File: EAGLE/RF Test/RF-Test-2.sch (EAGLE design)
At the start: 9 parts, among them X1 SMA-142-0701-881/886, X2 IPEX-20279-001E

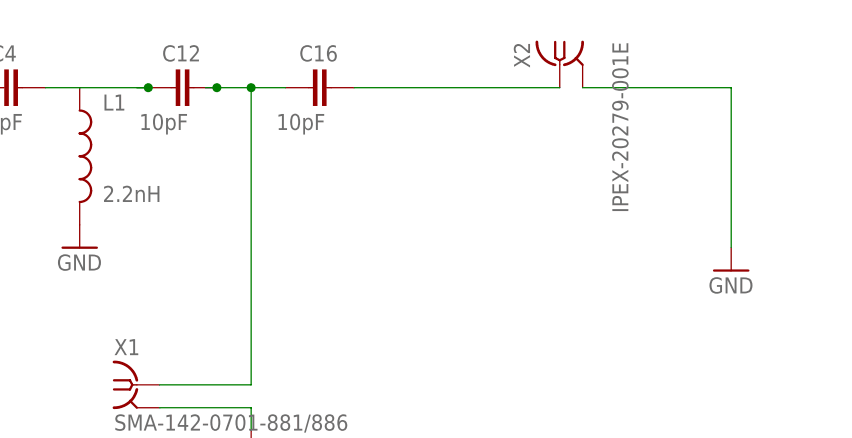
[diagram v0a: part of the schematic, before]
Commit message: RF Test board updated to match. A0 silk screen moved on core.
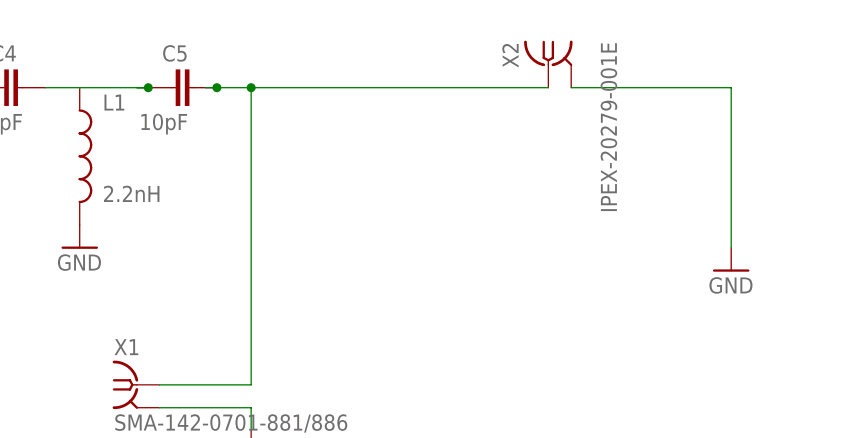
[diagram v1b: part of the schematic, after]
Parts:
- removed C16: 10pF, rcl:C-EUC0603
- renumbered C12 to C5
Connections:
- removed net N$2: C16.2, X2.1
- net N$4: now also X2.1; no longer C16.1
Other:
- moved on the sheet: X2
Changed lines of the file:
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@@
 <class number="1" name="vcc" width="0" drill="0">
 </class>
-<class number="2" name="RF" width="0.5842" drill="0">
-<clearance class="2" value="0.762"/>
+<class number="2" name="RF" width="0.635" drill="0">
+<clearance class="2" value="0.635"/>
 </class>
 <class number="3" name="RF2" width="0.5842" drill="0">
@@
 <part name="GND2" library="SparkFun" deviceset="GND" device=""/>
 <part name="X2" library="Spark" deviceset="IPEX-20279-001E" device=""/>
-<part name="C16" library="rcl" deviceset="C-EU" device="C0603" value="10pF"/>
 <part name="GND20" library="SparkFun" deviceset="GND" device=""/>
 <part name="ANT1" library="Spark" deviceset="AT8010" device=""/>
-<part name="C12" library="rcl" deviceset="C-EU" device="C0603" value="10pF"/>
+<part name="C5" library="rcl" deviceset="C-EU" device="C0603" value="10pF"/>
 <part name="X1" library="andyw-oct-2011" deviceset="SMA-" device="142-0701-881/886"/>
 <part name="GND1" library="SparkFun" deviceset="GND" device=""/>
@@
 </instance>
 <instance part="GND2" gate="1" x="113.03" y="104.14"/>
-<instance part="X2" gate="G$1" x="166.37" y="124.46" rot="MR270"/>
-<instance part="C16" gate="G$1" x="138.43" y="121.92" smashed="yes" rot="R90">
-<attribute name="NAME" x="137.414" y="124.841" size="1.778" layer="95"/>
-<attribute name="VALUE" x="134.874" y="117.221" size="1.778" layer="96"/>
-</instance>
+<instance part="X2" gate="G$1" x="165.1" y="124.46" rot="MR270"/>
 <instance part="GND20" gate="1" x="185.42" y="101.6"/>
 <instance part="ANT1" gate="G$1" x="92.71" y="121.92" rot="R90"/>
-<instance part="C12" gate="G$1" x="123.19" y="121.92" smashed="yes" rot="R90">
+<instance part="C5" gate="G$1" x="123.19" y="121.92" smashed="yes" rot="R90">
 <attribute name="NAME" x="122.174" y="124.841" size="1.778" layer="95"/>
 <attribute name="VALUE" x="119.634" y="117.221" size="1.778" layer="96"/>
@@
 <pinref part="X2" gate="G$1" pin="GND@1"/>
 <pinref part="GND20" gate="1" pin="GND"/>
-<wire x1="168.91" y1="121.92" x2="185.42" y2="121.92" width="0.1524" layer="91"/>
+<wire x1="167.64" y1="121.92" x2="185.42" y2="121.92" width="0.1524" layer="91"/>
 <wire x1="185.42" y1="121.92" x2="185.42" y2="104.14" width="0.1524" layer="91"/>
 </segment>
@@
 </segment>
 </net>
-<net name="N$4" class="3">
+<net name="N$4" class="2">
 <segment>
 <wire x1="132.08" y1="88.9" x2="132.08" y2="121.92" width="0.1524" layer="91"/>
-<pinref part="C16" gate="G$1" pin="1"/>
-<wire x1="135.89" y1="121.92" x2="132.08" y2="121.92" width="0.1524" layer="91"/>
 <wire x1="127" y1="121.92" x2="128.27" y2="121.92" width="0.1524" layer="91"/>
-<junction x="132.08" y="121.92"/>
-<pinref part="C12" gate="G$1" pin="2"/>
+<pinref part="C5" gate="G$1" pin="2"/>
 <wire x1="128.27" y1="121.92" x2="132.08" y2="121.92" width="0.1524" layer="91"/>
 <junction x="128.27" y="121.92"/>
 <pinref part="X1" gate="G1" pin="1"/>
 <wire x1="121.92" y1="88.9" x2="132.08" y2="88.9" width="0.1524" layer="91"/>
+<pinref part="X2" gate="G$1" pin="1"/>
+<wire x1="165.1" y1="121.92" x2="132.08" y2="121.92" width="0.1524" layer="91"/>
+<junction x="132.08" y="121.92"/>
 </segment>
 </net>
@@
 <wire x1="53.34" y1="68.58" x2="66.04" y2="68.58" width="0.1524" layer="91"/>
 <label x="60.96" y="68.58" size="1.778" layer="95"/>
-</segment>
-</net>
-<net name="N$2" class="2">
-<segment>
-<pinref part="C16" gate="G$1" pin="2"/>
-<pinref part="X2" gate="G$1" pin="1"/>
-<wire x1="143.51" y1="121.92" x2="166.37" y2="121.92" width="0.1524" layer="91"/>
 </segment>
 </net>
@@
 <wire x1="109.22" y1="121.92" x2="113.03" y2="121.92" width="0.1524" layer="91"/>
 <wire x1="119.38" y1="121.92" x2="120.65" y2="121.92" width="0.1524" layer="91"/>
-<pinref part="C12" gate="G$1" pin="1"/>
+<pinref part="C5" gate="G$1" pin="1"/>
 <wire x1="120.65" y1="121.92" x2="113.03" y2="121.92" width="0.1524" layer="91"/>
 <junction x="120.65" y="121.92"/>

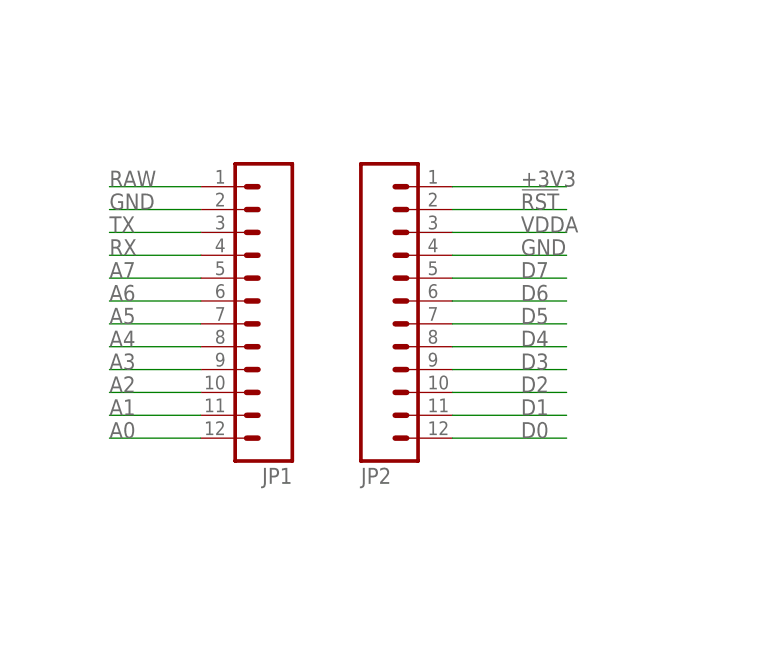
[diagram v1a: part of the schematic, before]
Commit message: Reduce stripline length, shorten test board.
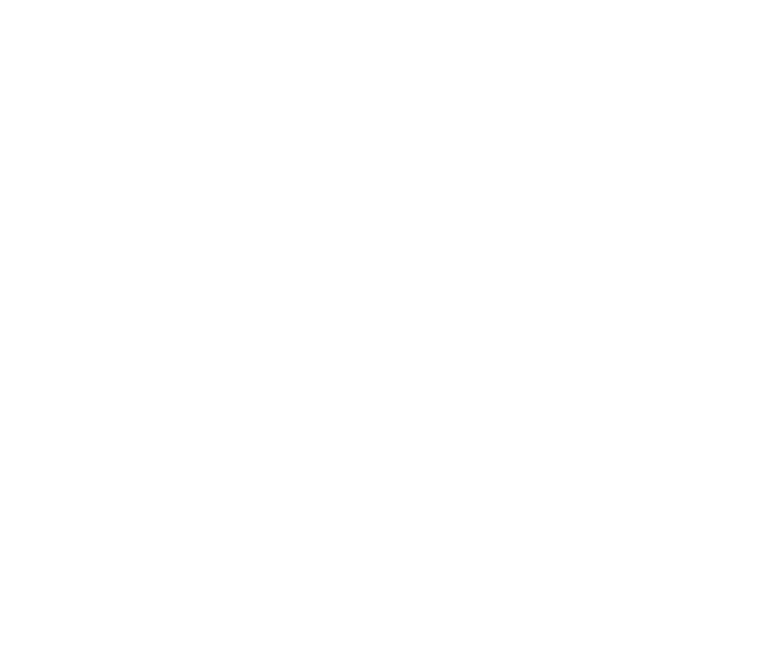
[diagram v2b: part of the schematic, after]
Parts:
- removed JP1, JP2: M12PTH, SparkFun:M12PTH
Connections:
- removed net !RST: JP2.2
- removed net +3V3: JP2.1
- removed net A0: JP1.12
- removed net A1: JP1.11
- removed net A2: JP1.10
- removed net A3: JP1.9
- removed net A4: JP1.8
- removed net A5: JP1.7
- removed net A6: JP1.6
- removed net A7: JP1.5
- removed net D0: JP2.12
- removed net D1: JP2.11
- removed net D2: JP2.10
- removed net D3: JP2.9
- removed net D4: JP2.8
- removed net D5: JP2.7
- removed net D6: JP2.6
- removed net D7: JP2.5
- removed net RAW: JP1.1
- removed net RX: JP1.4
- removed net TX: JP1.3
- removed net VDDA: JP2.3
- net GND: no longer JP1.2, JP2.4
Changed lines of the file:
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@@
 <parts>
 <part name="FRAME1" library="SparkFun" deviceset="FRAME-LETTER" device=""/>
-<part name="JP1" library="SparkFun" deviceset="M12" device="PTH" value=""/>
-<part name="JP2" library="SparkFun" deviceset="M12" device="PTH" value=""/>
 <part name="L1" library="SparkFun-Passives" deviceset="INDUCTOR" device="0603" value="2.2nH"/>
 <part name="C4" library="rcl" deviceset="C-EU" device="C0603" value="2.2pF"/>
@@
 <instance part="FRAME1" gate="G$1" x="0" y="0"/>
 <instance part="FRAME1" gate="G$2" x="147.32" y="0"/>
-<instance part="JP1" gate="G$1" x="35.56" y="58.42" rot="R180"/>
-<instance part="JP2" gate="G$1" x="43.18" y="58.42" rot="MR180"/>
 <instance part="L1" gate="G$1" x="113.03" y="114.3"/>
 <instance part="C4" gate="G$1" x="104.14" y="121.92" smashed="yes" rot="R90">
@@
 </segment>
 <segment>
-<pinref part="JP1" gate="G$1" pin="2"/>
-<wire x1="25.4" y1="71.12" x2="15.24" y2="71.12" width="0.1524" layer="91"/>
-<label x="15.24" y="71.12" size="1.778" layer="95"/>
-</segment>
-<segment>
-<pinref part="JP2" gate="G$1" pin="4"/>
-<wire x1="53.34" y1="66.04" x2="66.04" y2="66.04" width="0.1524" layer="91"/>
-<label x="60.96" y="66.04" size="1.778" layer="95"/>
-</segment>
-<segment>
 <pinref part="X2" gate="G$1" pin="GND@1"/>
 <pinref part="GND20" gate="1" pin="GND"/>
@@
 <wire x1="121.92" y1="86.36" x2="132.08" y2="86.36" width="0.1524" layer="91"/>
 <wire x1="132.08" y1="86.36" x2="132.08" y2="83.82" width="0.1524" layer="91"/>
-</segment>
-</net>
-<net name="RAW" class="1">
-<segment>
-<wire x1="25.4" y1="73.66" x2="15.24" y2="73.66" width="0.1524" layer="91"/>
-<label x="15.24" y="73.66" size="1.778" layer="95"/>
-<pinref part="JP1" gate="G$1" pin="1"/>
-</segment>
-</net>
-<net name="+3V3" class="0">
-<segment>
-<pinref part="JP2" gate="G$1" pin="1"/>
-<wire x1="53.34" y1="73.66" x2="66.04" y2="73.66" width="0.1524" layer="91"/>
-<label x="60.96" y="73.66" size="1.778" layer="95"/>
-</segment>
-</net>
-<net name="D4" class="0">
-<segment>
-<pinref part="JP2" gate="G$1" pin="8"/>
-<wire x1="53.34" y1="55.88" x2="66.04" y2="55.88" width="0.1524" layer="91"/>
-<label x="60.96" y="55.88" size="1.778" layer="95"/>
-</segment>
-</net>
-<net name="D2" class="0">
-<segment>
-<pinref part="JP2" gate="G$1" pin="10"/>
-<wire x1="53.34" y1="50.8" x2="66.04" y2="50.8" width="0.1524" layer="91"/>
-<label x="60.96" y="50.8" size="1.778" layer="95"/>
-</segment>
-</net>
-<net name="D0" class="0">
-<segment>
-<pinref part="JP2" gate="G$1" pin="12"/>
-<wire x1="53.34" y1="45.72" x2="66.04" y2="45.72" width="0.1524" layer="91"/>
-<label x="60.96" y="45.72" size="1.778" layer="95"/>
-</segment>
-</net>
-<net name="D1" class="0">
-<segment>
-<pinref part="JP2" gate="G$1" pin="11"/>
-<wire x1="53.34" y1="48.26" x2="66.04" y2="48.26" width="0.1524" layer="91"/>
-<label x="60.96" y="48.26" size="1.778" layer="95"/>
-</segment>
-</net>
-<net name="D3" class="0">
-<segment>
-<pinref part="JP2" gate="G$1" pin="9"/>
-<wire x1="53.34" y1="53.34" x2="66.04" y2="53.34" width="0.1524" layer="91"/>
-<label x="60.96" y="53.34" size="1.778" layer="95"/>
 </segment>
 </net>
@@
 </segment>
 </net>
-<net name="!RST" class="0">
-<segment>
-<pinref part="JP2" gate="G$1" pin="2"/>
-<wire x1="53.34" y1="71.12" x2="66.04" y2="71.12" width="0.1524" layer="91"/>
-<label x="60.96" y="71.12" size="1.778" layer="95"/>
-</segment>
-</net>
-<net name="A0" class="0">
-<segment>
-<pinref part="JP1" gate="G$1" pin="12"/>
-<wire x1="25.4" y1="45.72" x2="15.24" y2="45.72" width="0.1524" layer="91"/>
-<label x="15.24" y="45.72" size="1.778" layer="95"/>
-</segment>
-</net>
-<net name="A1" class="0">
-<segment>
-<pinref part="JP1" gate="G$1" pin="11"/>
-<wire x1="25.4" y1="48.26" x2="15.24" y2="48.26" width="0.1524" layer="91"/>
-<label x="15.24" y="48.26" size="1.778" layer="95"/>
-</segment>
-</net>
-<net name="TX" class="0">
-<segment>
-<pinref part="JP1" gate="G$1" pin="3"/>
-<wire x1="25.4" y1="68.58" x2="15.24" y2="68.58" width="0.1524" layer="91"/>
-<label x="15.24" y="68.58" size="1.778" layer="95"/>
-</segment>
-</net>
-<net name="RX" class="0">
-<segment>
-<pinref part="JP1" gate="G$1" pin="4"/>
-<wire x1="25.4" y1="66.04" x2="15.24" y2="66.04" width="0.1524" layer="91"/>
-<label x="15.24" y="66.04" size="1.778" layer="95"/>
-</segment>
-</net>
-<net name="A2" class="0">
-<segment>
-<pinref part="JP1" gate="G$1" pin="10"/>
-<wire x1="25.4" y1="50.8" x2="15.24" y2="50.8" width="0.1524" layer="91"/>
-<label x="15.24" y="50.8" size="1.778" layer="95"/>
-</segment>
-</net>
-<net name="A3" class="0">
-<segment>
-<pinref part="JP1" gate="G$1" pin="9"/>
-<wire x1="25.4" y1="53.34" x2="15.24" y2="53.34" width="0.1524" layer="91"/>
-<label x="15.24" y="53.34" size="1.778" layer="95"/>
-</segment>
-</net>
-<net name="A4" class="0">
-<segment>
-<pinref part="JP1" gate="G$1" pin="8"/>
-<wire x1="25.4" y1="55.88" x2="15.24" y2="55.88" width="0.1524" layer="91"/>
-<label x="15.24" y="55.88" size="1.778" layer="95"/>
-</segment>
-</net>
-<net name="A5" class="0">
-<segment>
-<pinref part="JP1" gate="G$1" pin="7"/>
-<wire x1="25.4" y1="58.42" x2="15.24" y2="58.42" width="0.1524" layer="91"/>
-<label x="15.24" y="58.42" size="1.778" layer="95"/>
-</segment>
-</net>
-<net name="A6" class="0">
-<segment>
-<pinref part="JP1" gate="G$1" pin="6"/>
-<wire x1="25.4" y1="60.96" x2="15.24" y2="60.96" width="0.1524" layer="91"/>
-<label x="15.24" y="60.96" size="1.778" layer="95"/>
-</segment>
-</net>
-<net name="A7" class="0">
-<segment>
-<pinref part="JP1" gate="G$1" pin="5"/>
-<wire x1="25.4" y1="63.5" x2="15.24" y2="63.5" width="0.1524" layer="91"/>
-<label x="15.24" y="63.5" size="1.778" layer="95"/>
-</segment>
-</net>
-<net name="D5" class="0">
-<segment>
-<pinref part="JP2" gate="G$1" pin="7"/>
-<wire x1="53.34" y1="58.42" x2="66.04" y2="58.42" width="0.1524" layer="91"/>
-<label x="60.96" y="58.42" size="1.778" layer="95"/>
-</segment>
-</net>
-<net name="D6" class="0">
-<segment>
-<pinref part="JP2" gate="G$1" pin="6"/>
-<wire x1="53.34" y1="60.96" x2="66.04" y2="60.96" width="0.1524" layer="91"/>
-<label x="60.96" y="60.96" size="1.778" layer="95"/>
-</segment>
-</net>
-<net name="D7" class="0">
-<segment>
-<pinref part="JP2" gate="G$1" pin="5"/>
-<wire x1="53.34" y1="63.5" x2="66.04" y2="63.5" width="0.1524" layer="91"/>
-<label x="60.96" y="63.5" size="1.778" layer="95"/>
-</segment>
-</net>
-<net name="VDDA" class="0">
-<segment>
-<pinref part="JP2" gate="G$1" pin="3"/>
-<wire x1="53.34" y1="68.58" x2="66.04" y2="68.58" width="0.1524" layer="91"/>
-<label x="60.96" y="68.58" size="1.778" layer="95"/>
-</segment>
-</net>
